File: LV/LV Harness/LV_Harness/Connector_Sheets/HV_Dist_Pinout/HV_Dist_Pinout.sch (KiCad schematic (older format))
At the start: 2 parts

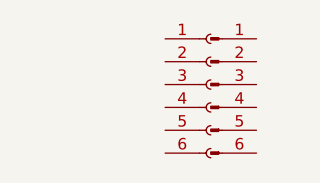
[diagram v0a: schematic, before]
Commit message: Changes to LV Harness Folders
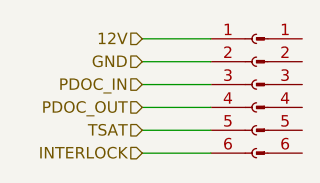
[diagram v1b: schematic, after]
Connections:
- net 12V: now reaches J?.1 (Pin_1)
- net GND: now reaches J?.2 (Pin_2)
- net PDOC_IN: now reaches J?.3 (Pin_3)
- net PDOC_OUT: now reaches J?.4 (Pin_4)
- net TSAT: now reaches J?.5 (Pin_5)
- net INTERLOCK: now reaches J?.6 (Pin_6)
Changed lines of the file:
@@
 EESchema Schematic File Version 4
+LIBS:HV_Dist_Pinout-cache
 EELAYER 29 0
 EELAYER END
@@
 L Connector:Conn_01x06_Female J?
 U 1 1 60F25ED0
-P 5000 3250
-F 0 "J?" H 4850 3600 50  0001 L CNN
-F 1 "Conn_01x06_Female" H 4300 2850 50  0001 L CNN
-F 2 "" H 5000 3250 50  0001 C CNN
-F 3 "~" H 5000 3250 50  0001 C CNN
-	1    5000 3250
+P 5200 3250
+F 0 "J?" H 5050 3600 50  0001 L CNN
+F 1 "Conn_01x06_Female" H 4500 2850 50  0001 L CNN
+F 2 "" H 5200 3250 50  0001 C CNN
+F 3 "~" H 5200 3250 50  0001 C CNN
+	1    5200 3250
 	1    0    0    -1
 $EndComp
@@
 L Connector:Conn_01x06_Male J?
 U 1 1 60F26938
-P 5000 3250
-F 0 "J?" H 5100 3600 50  0001 C CNN
-F 1 "Conn_01x06_Male" H 5350 2850 50  0001 C CNN
-F 2 "" H 5000 3250 50  0001 C CNN
-F 3 "~" H 5000 3250 50  0001 C CNN
-	1    5000 3250
+P 5200 3250
+F 0 "J?" H 5300 3600 50  0001 C CNN
+F 1 "Conn_01x06_Male" H 5550 2850 50  0001 C CNN
+F 2 "" H 5200 3250 50  0001 C CNN
+F 3 "~" H 5200 3250 50  0001 C CNN
+	1    5200 3250
 	1    0    0    -1
 $EndComp
+Text HLabel 4700 3050 0    50   Input ~ 0
+12V
+Text HLabel 4700 3150 0    50   Input ~ 0
+GND
+Text HLabel 4700 3250 0    50   Input ~ 0
+PDOC_IN
+Text HLabel 4700 3350 0    50   Input ~ 0
+PDOC_OUT
+Text HLabel 4700 3450 0    50   Input ~ 0
+TSAT
+Text HLabel 4700 3550 0    50   Input ~ 0
+INTERLOCK
+Wire Wire Line
+	4700 3050 5000 3050
+Wire Wire Line
+	5000 3150 4700 3150
+Wire Wire Line
+	4700 3250 5000 3250
+Wire Wire Line
+	5000 3350 4700 3350
+Wire Wire Line
+	4700 3450 5000 3450
+Wire Wire Line
+	5000 3550 4700 3550
 $EndSCHEMATC
